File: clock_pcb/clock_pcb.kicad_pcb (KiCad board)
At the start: 2 copper layers, 90 parts, among them J2 PROG, J3 FFC 24, J4 SM02B, J5 OLED, Q1 AO3401A, Q2 AO3401A, SW1 TS-1187A-B-A-B, SW3 TS-1187A-B-A-B, SW4 TS-1187A-B-A-B, SW5 TS-1187A-B-A-B, U1 SRV05-4, U3 RT9080-33GJ5, U4 W25Q64JV, U5 DS1307Z+, Y1 XYDBPCNANF-12MHZ, Y2 32.768kHz

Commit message: break
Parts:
- removed the C23 at (174.6, 87.7)
- removed the C5 at (113.9, 95.2)
- removed the J5 at (157.4, 84.4)
- added BT1: CR2032, ftp:Q&J_CR2032-BS-6-1, F.Cu at (60.2, 148.5)
- added C25: 1u, Capacitor_SMD:C_0402_1005Metric, F.Cu at (121.0, 96.0)
- added C30: 0.1u, Capacitor_SMD:C_0402_1005Metric, F.Cu at (118.1, 100.0)
- added D5: WS2812B-2020, ftp:WS2812B-2020, F.Cu at (92.1, 162.2)
- added H1: Tooling_Hole_JLC, ftp:JLC_Tooling_Hole, F.Cu at (57.0, 149.0)
- added H2: Tooling_Hole_JLC, ftp:JLC_Tooling_Hole, F.Cu at (57.0, 116.1)
- added H3: Tooling_Hole_JLC, ftp:JLC_Tooling_Hole, F.Cu at (143.0, 116.0)
- added J1: USB_C_Receptacle_USB2.0, ftp:USB-C-16p, F.Cu at (142.3, 132.4)
- added J4: 5V, Connector_JST:JST_SH_SM02B-SRSS-TB_1x02-1MP_P1.00mm_Horizontal, F.Cu at (115.0, 119.0)
- added J6: OLED, ftp:OLED-128O064D_edit, F.Cu at (85.1, 132.5)
- added Q3: 2N7002, Package_TO_SOT_SMD:SOT-23, F.Cu at (95.8, 166.5)
- added R24: 10k, Resistor_SMD:R_0402_1005Metric, F.Cu at (77.5, 118.2)
- added R25: 10k, Resistor_SMD:R_0402_1005Metric, F.Cu at (95.8, 169.2)
- added R27: 10k, Resistor_SMD:R_0402_1005Metric, F.Cu at (118.1, 96.0)
- added R28: 1k, Resistor_SMD:R_0402_1005Metric, F.Cu at (118.1, 98.0)
- added SW2: SSSS811101, ftp:SSSS811101, F.Cu at (125.0, 118.0)
- added U2: RP2040, ftp:QFN-56_EP_7x7_Pitch0.4mm, F.Cu at (107.0, 173.0)
- D1: value IO -> LED
- D3: value 5V Blue -> LED
- D4: value 3V3 Blue -> LED
- H4, H5, H6, H7: footprint MountingHole:MountingHole_3.2mm_M3 -> MountingHole:MountingHole_2.7mm_M2.5
- J5: renamed from J4; value SM02B -> 5V
- R22: value 0 -> 10k
- TP1: value 5V -> VBUS
- TP2: value 5V -> GND
- TP3: value 5V -> RST
- TP6: value 5V -> 3V3
- moved C31 116.3 mm to (90.6, 189.3), turned to 180 degrees
- moved C27 115.5 mm to (90.6, 190.6), turned to 180 degrees
- moved C21 111.4 mm to (94.2, 162.3), turned to 90 degrees
- moved R3 109.8 mm to (100.6, 183.7), turned to 180 degrees
- moved TP3 108.4 mm to (98.3, 183.7), turned to 180 degrees
- moved C26 105.0 mm to (88.5, 137.1)
- moved C11 103.3 mm to (110.7, 178.8), turned to -90 degrees
- moved C20 103.3 mm to (74.7, 115.7), turned to 180 degrees
- moved R22 102.6 mm to (92.9, 165.4), turned to -90 degrees
- moved J2 102.2 mm to (94.9, 181.4), turned to 90 degrees
- moved R5 101.4 mm to (115.3, 181.8), turned to 180 degrees
- moved U5 100.9 mm to (72.7, 119.5)
- moved R20 100.9 mm to (91.3, 165.4), turned to -90 degrees
- moved C13 100.1 mm to (100.5, 175.3)
- moved C7 100.1 mm to (106.0, 178.8), turned to -90 degrees
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- renumbered C11 to C10, C12 to C11, C13 to C12, C14 to C13, C15 to C14, C16 to C15, C17 to C16, C18 to C17, C19 to C18, C20 to C19, C21 to C20, C22 to C21, C24 to C22, C25 to C23, C26 to C24, C27 to C26, C28 to C27, C29 to C28, C30 to C29, C6 to C5, C7 to C6, C8 to C7, C9 to C8, C10 to C9, R21 to R20, R20 to R21, R24 to R26, R25 to R29, R4 to R3, R5 to R4, R3 to R5
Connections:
- net /PAGE3/OLED_RES renamed /PAGE3/OLED_RST
- C19 pad 1: /PAGE3/SPI_MISO -> BUTTON_0
- C22 pad 1: /PAGE3/SPI_MOSI -> BUTTON_1
- D1 pad 1: /PAGE2/GPIO25 -> GND
- J3 pad 10: /PAGE3/TX -> GPIO4
- J3 pad 11: /PAGE3/GPIO2 -> GPIO5
- J3 pad 12: /PAGE3/RX -> GPIO6
- J3 pad 13: /PAGE3/GPIO4 -> GND
- J3 pad 14: /PAGE3/GPIO5 -> GPIO7
- J3 pad 15: GND -> GPIO8
- J3 pad 16: /PAGE3/SPI_MISO -> GPIO9
- J3 pad 17: /PAGE3/SPI_MOSI -> GPIO10
- J3 pad 18: /PAGE3/SPI_SCLK -> GND
- J3 pad 19: /PAGE3/SPI_SS -> GPIO27_ADC1
- J3 pad 20: /PAGE3/GPIO16 -> GPIO28_ADC2
- J3 pad 21: /PAGE3/WS2812_DOUT -> GND
- J3 pad 22: GND -> I2C_SDA
- J3 pad 23: unconnected-(J3-Pad23) -> I2C_SCL
- J3 pad 24: unconnected-(J3-Pad24) -> GND
- J3 pad 5: unconnected-(J3-Pad5) -> GND
- J3 pad 6: unconnected-(J3-Pad6) -> /PAGE3/WS2812_DOUT
- J3 pad 7: GND -> PPS
- J3 pad 8: /PAGE3/ADC_3V3 -> GPIO2
- J3 pad 9: /PAGE3/GPIO0 -> GPIO3
- J5 pad 2: +5V -> PWR_OFF_SW_N
- R13 pad 1: /PAGE2/I2C0_SCL -> I2C_SCL
- R14 pad 1: /PAGE2/I2C0_SDA -> I2C_SDA
- R18 pad 2: /PAGE3/SPI_MISO -> BUTTON_0
- R19 pad 2: /PAGE3/SPI_MISO -> BUTTON_0
- R20 pad 2: /PAGE3/GPIO2 -> Net-(Q3-Pad3)
- R21 pad 2: /PAGE3/SPI_MOSI -> BUTTON_1
- R22 pad 1: Net-(R22-Pad1) -> +5V
- R22 pad 2: /PAGE3/SPI_SCLK -> Net-(Q3-Pad3)
- R23 pad 2: /PAGE3/SPI_MOSI -> BUTTON_1
- R5 pad 2: +3V3 -> /PAGE2/GPIO25_LED
- R8 pad 2: Net-(R8-Pad2) -> PWR_OFF_SW_N
- R9 pad 2: Net-(R8-Pad2) -> PWR_OFF_SW_N
- U1 pad 1: /PAGE2/USB_D+ -> /PAGE2/USB_D-
- U1 pad 3: /PAGE2/USB_D- -> /PAGE2/USB_D+
- U5 pad 5: /PAGE3/GPIO4 -> I2C_SDA
- U5 pad 6: /PAGE3/GPIO5 -> I2C_SCL
- U5 pad 7: Net-(R22-Pad1) -> PPS
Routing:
- net Net-(C12-Pad2): track 0.00 -> 2.36 mm
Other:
- board outline added: 100 x 35 mm
- board text added: "0"
- board text added: "3V3"
- board text added: "5V"
- board text added: "I"
- board text added: "I2C"
- board text added: "OFF"
- board text added: "ON"
- board text added: "PWR"
- board text added: "RESET"
- board text added: "RST"
- board text added: "SWITCH"
- board text added: "USB BOOT"
- board text added: "VBUS"

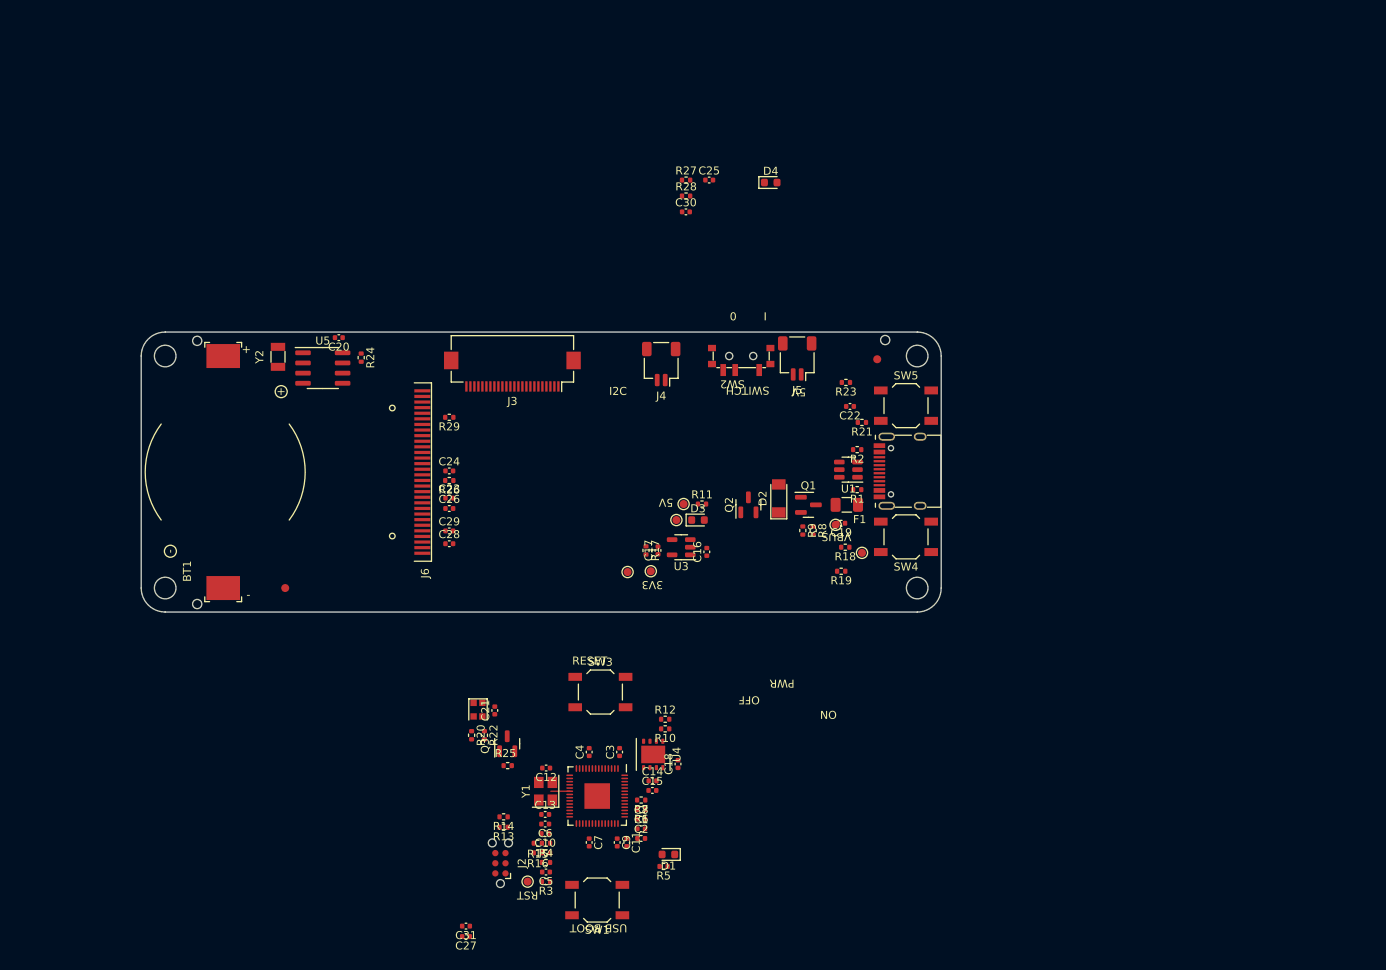
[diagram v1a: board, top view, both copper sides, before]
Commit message: only brick nogging usbc left to add
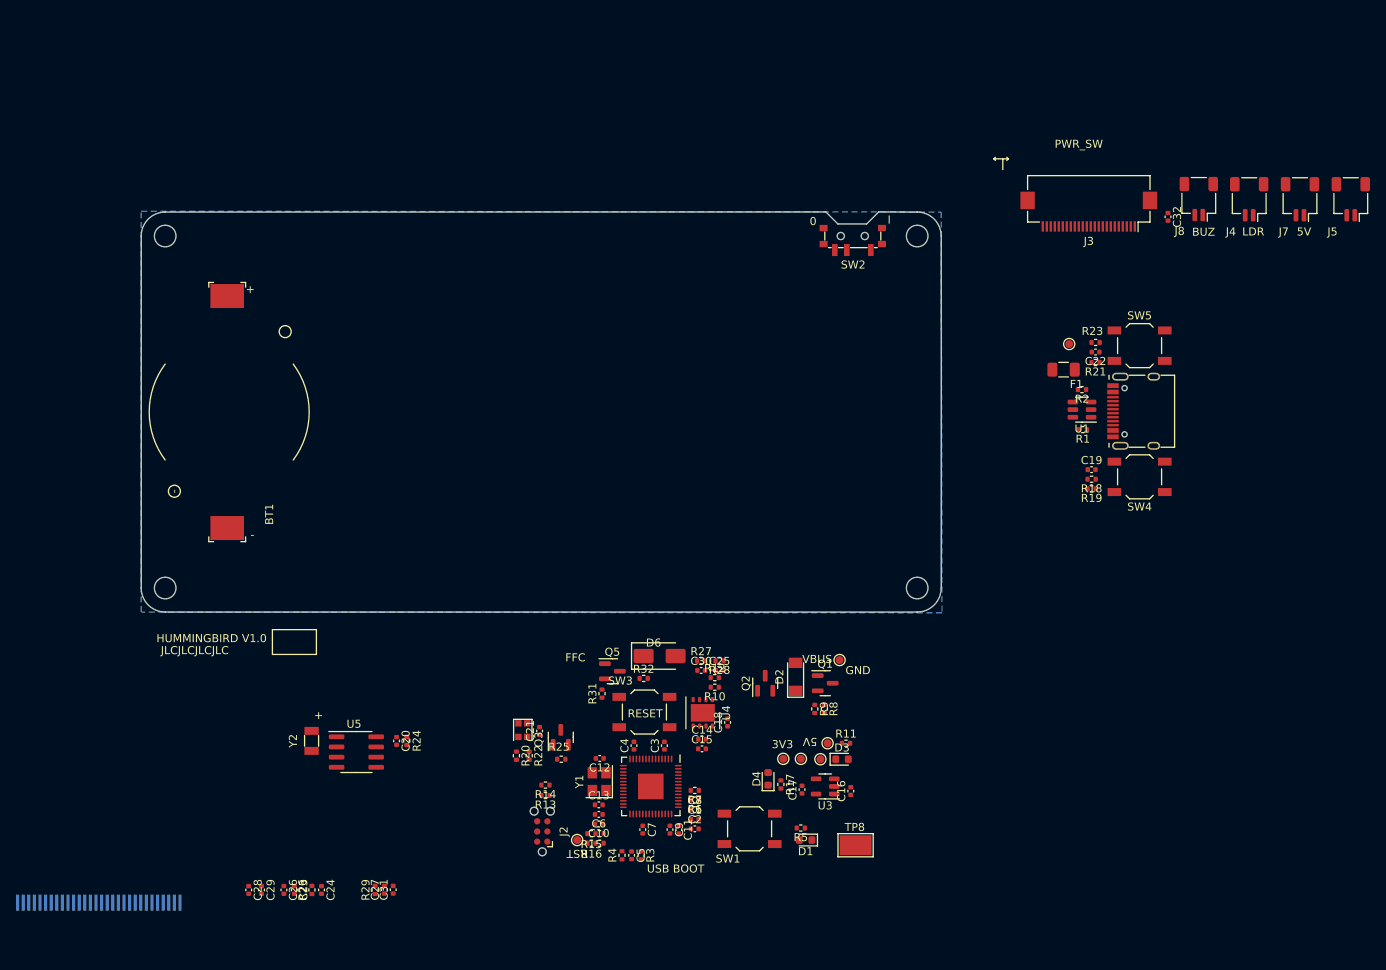
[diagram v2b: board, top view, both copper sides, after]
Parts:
- removed FID1, FID2: Fiducial, Fiducial:Fiducial_1mm_Mask2mm
- removed H1, H2, H3: Tooling_Hole_JLC, ftp:JLC_Tooling_Hole
- added C32: 10u, Capacitor_SMD:C_0402_1005Metric, F.Cu at (178.3, 100.6)
- added D6: SS14, Diode_SMD:D_SMA, F.Cu at (114.8, 155.5)
- added J7: 5V, Connector_JST:JST_SH_SM02B-SRSS-TB_1x02-1MP_P1.00mm_Horizontal, F.Cu at (194.8, 98.4)
- added J8: 5V, Connector_JST:JST_SH_SM02B-SRSS-TB_1x02-1MP_P1.00mm_Horizontal, F.Cu at (182.2, 98.4)
- added Q5: AO3400A, Package_TO_SOT_SMD:SOT-23, F.Cu at (108.9, 157.4)
- added R31: 10k, Resistor_SMD:R_0402_1005Metric, F.Cu at (107.6, 160.2)
- added R32: 120, Resistor_SMD:R_0402_1005Metric, F.Cu at (112.8, 158.3)
- added TP8: GND CLIP, Mitch_Library:ronghe_RH-5016_C5199799, F.Cu at (139.2, 179.4)
- J6: footprint ftp:OLED-128O064D_edit -> Mitch_Library:OLED-128O064D_edit_reverse; moved to B.Cu
- moved J4 76.3 mm to (188.5, 98.4)
- moved J3 74.8 mm to (168.4, 100.0)
- moved D4 74.5 mm to (128.4, 170.8), turned to 90 degrees
- moved J5 72.0 mm to (201.2, 98.4)
- moved J6 67.3 mm to (44.7, 186.3), turned to 0 degrees
- moved C25 61.3 mm to (122.3, 157.3)
- moved R27 60.1 mm to (120.0, 156.1)
- moved R29 59.8 mm to (79.2, 184.7), turned to 90 degrees
- moved R28 58.3 mm to (122.3, 156.1), turned to 180 degrees
- moved C30 57.4 mm to (120.0, 157.3)
- moved C24 54.8 mm to (72.5, 184.7), turned to -90 degrees
- moved R26 54.0 mm to (71.3, 184.7), turned to 90 degrees
- moved C23 52.7 mm to (69.1, 184.7), turned to -90 degrees
- moved C26 52.0 mm to (67.8, 184.7), turned to -90 degrees
- moved C20 50.9 mm to (81.9, 166.1), turned to -90 degrees
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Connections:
- J3 pad MP: (no net) -> GND
- J4 pad MP: (no net) -> GND
- J5 pad MP: (no net) -> GND
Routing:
- net Net-(U2-XIN): track 2.36 -> 0.00 mm
- added copper zone on B.Cu, net GND
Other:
- board size 100 x 35 mm -> 100 x 50 mm
- board text added: "BUZ"
- board text added: "FFC"
- board text added: "GND"
- board text added: "HUMMINGBIRD V1.0"
- board text added: "JLCJLCJLCJLC"
- board text added: "LDR"
- board text added: "PWR_SW"
- board text removed: "I2C"
- board text removed: "OFF"
- board text removed: "ON"
- board text removed: "PWR"
- board text removed: "SWITCH"
